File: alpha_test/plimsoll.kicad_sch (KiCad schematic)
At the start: 46 parts, among them J1 TAG CONNECT, J2 USB_C, J3 Loadd Cell, J4 Test Points, SW1 RESET, SW2 BOOT0, U1 USBLC6-2SC6, U2 APX803L20-29SA-7, U3 STM32F072RBTx, U4 AP2205-3.3, U5 RS3236-3.3, U6 HX717

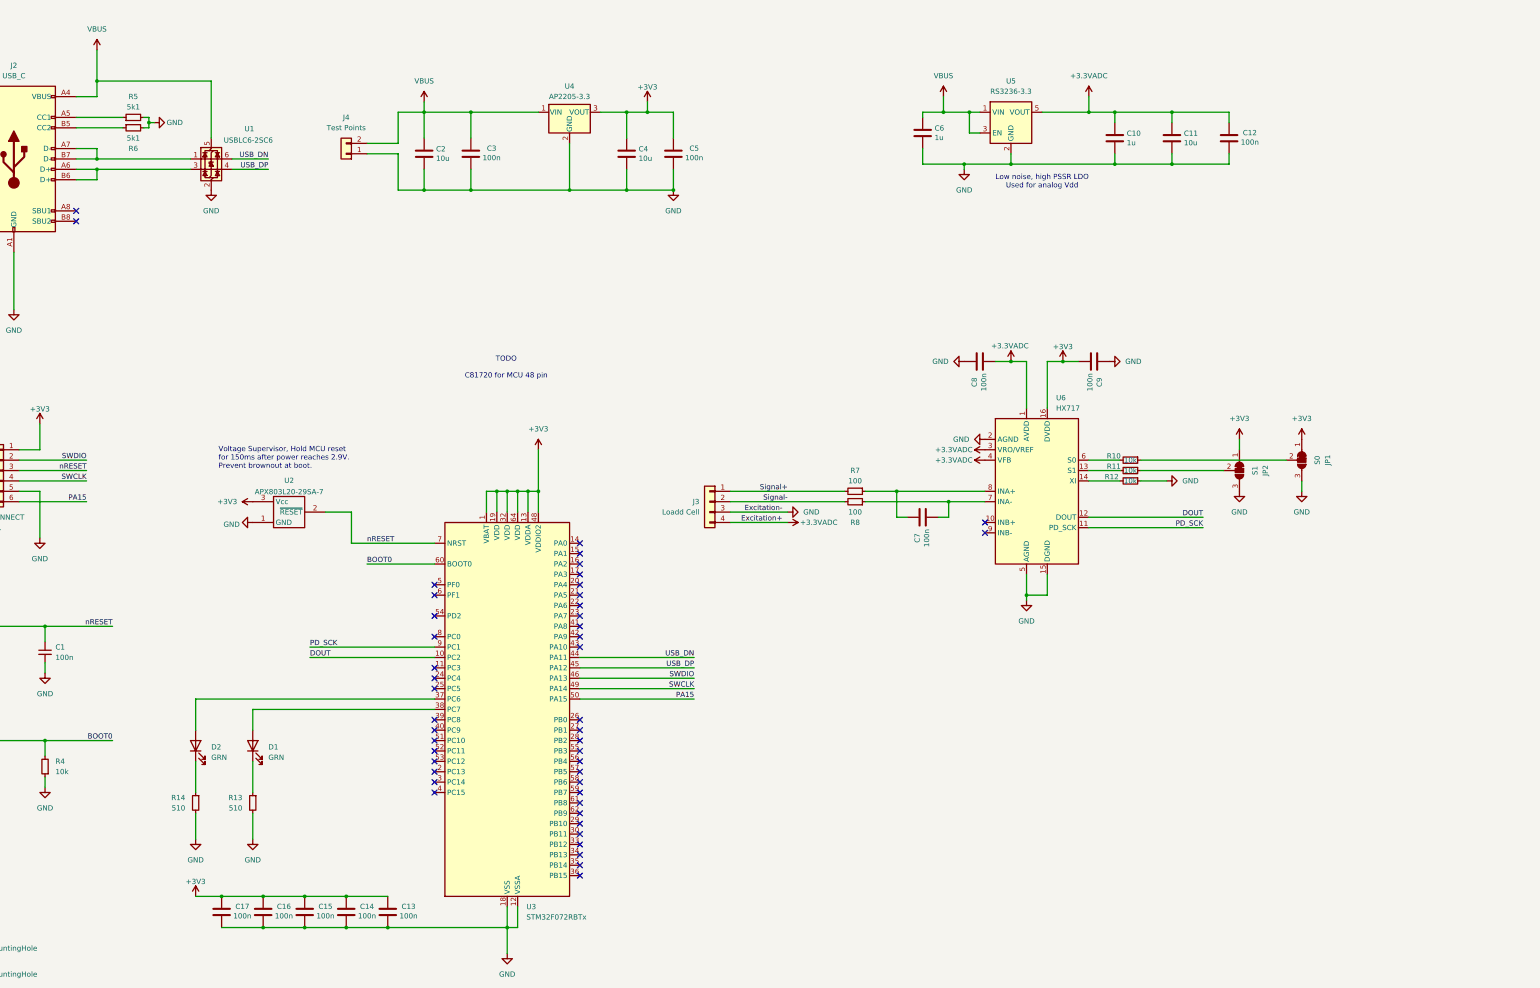
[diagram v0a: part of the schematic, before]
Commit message: updated alpha test for pcb to reuse parts from the alpha test
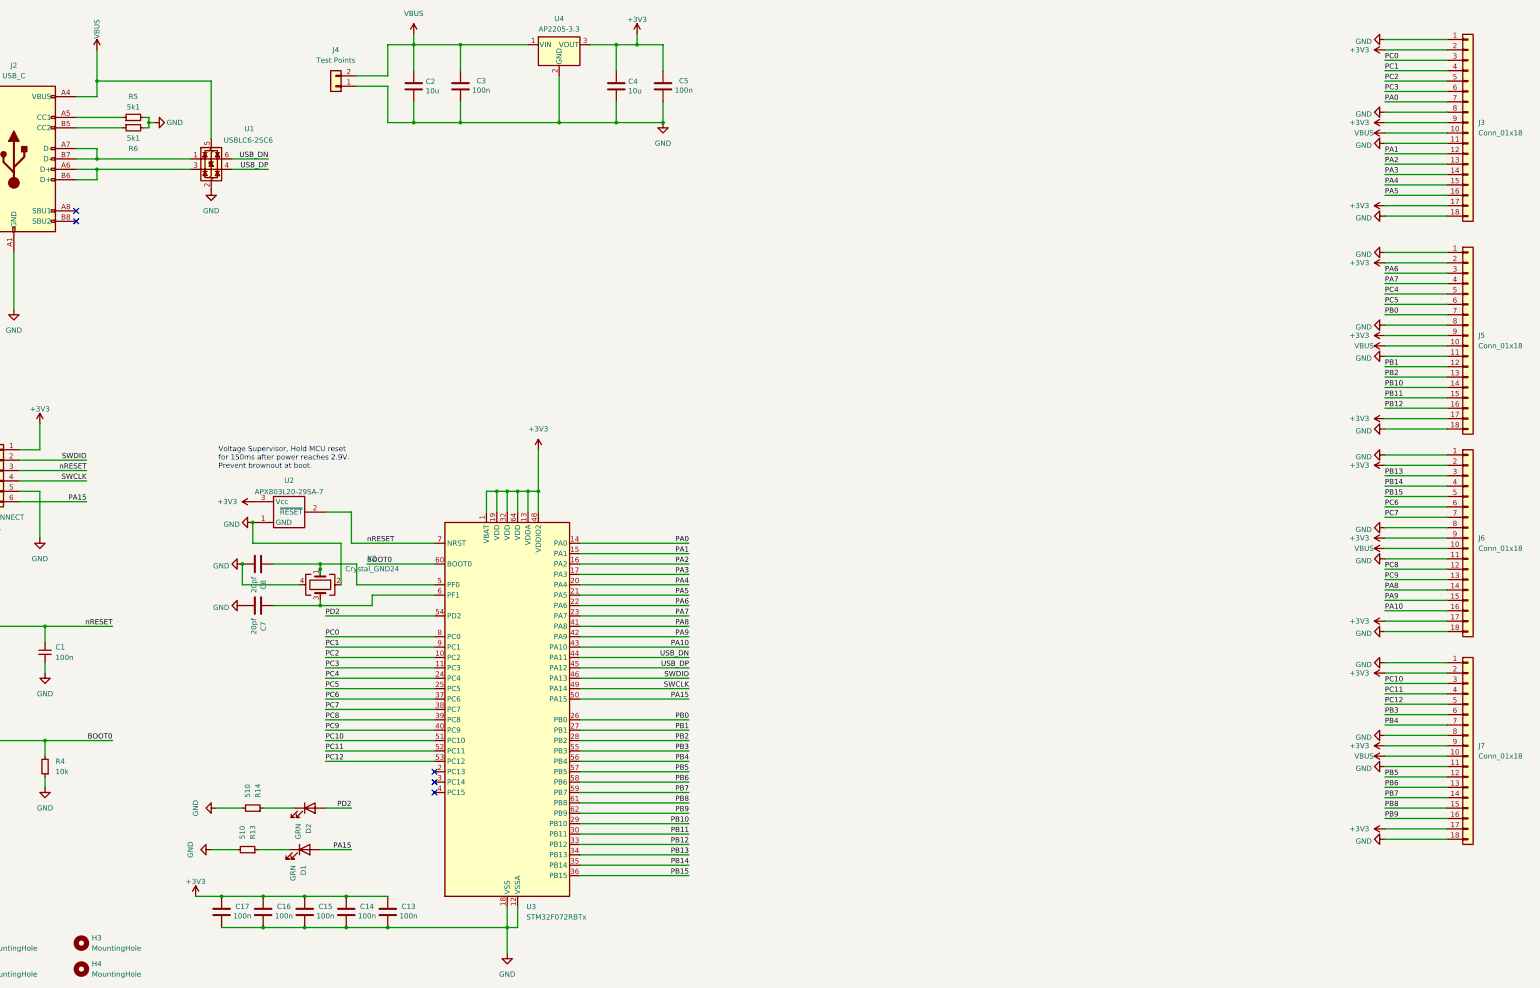
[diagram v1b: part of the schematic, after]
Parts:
- removed C10, C6: 1u, Capacitor_SMD:C_0805_2012Metric, symbol Device:C
- removed C11: 10u, Capacitor_SMD:C_0805_2012Metric, symbol Device:C
- removed C12, C9: 100n, Capacitor_SMD:C_0603_1608Metric, symbol Device:C
- removed J3: Loadd Cell, Connector_JST:JST_XH_B4B-XH-A_1x04_P2.50mm_Vertical, symbol Connector_Generic:Conn_01x04
- removed JP1: S0, Jumper:SolderJumper-3_P1.3mm_Bridged12_RoundedPad1.0x1.5mm_NumberLabels, symbol Jumper:SolderJumper_3_Bridged12
- removed JP2: S1, Jumper:SolderJumper-3_P1.3mm_Bridged12_RoundedPad1.0x1.5mm_NumberLabels, symbol Jumper:SolderJumper_3_Bridged12
- removed R10, R11, R12: 10k, Resistor_SMD:R_0603_1608Metric, symbol Device:R_Small
- removed R7, R8: 100, Resistor_SMD:R_0603_1608Metric, symbol Device:R_Small
- removed U5: RS3236-3.3, Package_TO_SOT_SMD:SOT-23-5, symbol Regulator_Linear:NCP163ASN350T1G
- removed U6: HX717, Package_SO:SOP-16_3.9x9.9mm_P1.27mm, symbol plimsoll-symbols:HX717
- added H3, H4: MountingHole, MountingHole:MountingHole_2.2mm_M2_ISO7380, symbol Mechanical:MountingHole
- added J3, J5, J6, J7: Conn_01x18, Connector_PinHeader_2.54mm:PinHeader_1x18_P2.54mm_Vertical, symbol Connector_Generic:Conn_01x18
- added Y2: Crystal_GND24, Crystal:Crystal_SMD_3225-4Pin_3.2x2.5mm_HandSoldering, symbol Device:Crystal_GND24
- C7, C8: value 100n -> 20pf
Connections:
- net +3.3VADC is gone; now on net GND: C8.1
- net +3V3: now also J3.17 (Pin_17), J3.2 (Pin_2), J3.9 (Pin_9), J5.17 (Pin_17), J5.2 (Pin_2), J5.9 (Pin_9), J6.17 (Pin_17), J6.2 (Pin_2), J6.9 (Pin_9), J7.17 (Pin_17), J7.2 (Pin_2), J7.9 (Pin_9)
- net GND: now also C7.1, J3.1 (Pin_1), J3.11 (Pin_11), J3.18 (Pin_18), J3.8 (Pin_8), J5.1 (Pin_1), J5.11 (Pin_11), J5.18 (Pin_18), J5.8 (Pin_8), J6.1 (Pin_1), J6.11 (Pin_11), J6.18 (Pin_18), J6.8 (Pin_8), J7.1 (Pin_1), J7.11 (Pin_11), J7.18 (Pin_18), J7.8 (Pin_8), Y2.2, Y2.4; no longer C8.2
- net PA15: now also D1.2 (A)
- net VBUS: now also J3.10 (Pin_10), J5.10 (Pin_10), J6.10 (Pin_10), J7.10 (Pin_10)
- net PC6: now reaches U3.37 (PC6)
- net PC6: now also J6.6 (Pin_6); no longer D2.2 (A)
- net at C7.2: now also U3.6 (PF1), Y2.3
- net PC3: now reaches U3.11 (PC3)
- net PC3: now also J3.6 (Pin_6)
- net PA0: now reaches U3.14 (PA0)
- net PA0: now also J3.7 (Pin_7)
- net PA1: now reaches U3.15 (PA1)
- net PA1: now also J3.12 (Pin_12)
- net PA2: now reaches U3.16 (PA2)
- net PA2: now also J3.13 (Pin_13)
- net PA3: now reaches U3.17 (PA3)
- net PA3: now also J3.14 (Pin_14)
- net PA4: now reaches U3.20 (PA4)
- net PA4: now also J3.15 (Pin_15)
- net PA5: now reaches U3.21 (PA5)
- net PA5: now also J3.16 (Pin_16)
- net PA6: now reaches U3.22 (PA6)
- net PA6: now also J5.3 (Pin_3)
- net PA7: now reaches U3.23 (PA7)
- net PA7: now also J5.4 (Pin_4)
- net PC4: now reaches U3.24 (PC4)
- net PC4: now also J5.5 (Pin_5)
- net PC5: now reaches U3.25 (PC5)
- net PC5: now also J5.6 (Pin_6)
- net PB0: now reaches U3.26 (PB0)
- net PB0: now also J5.7 (Pin_7)
- net PB1: now reaches U3.27 (PB1)
- net PB1: now also J5.12 (Pin_12)
- net PB2: now reaches U3.28 (PB2)
- net PB2: now also J5.13 (Pin_13)
- net PB10: now reaches U3.29 (PB10)
- net PB10: now also J5.14 (Pin_14)
- net PB11: now reaches U3.30 (PB11)
- net PB11: now also J5.15 (Pin_15)
- net PB12: now reaches U3.33 (PB12)
- net PB12: now also J5.16 (Pin_16)
- net PB13: now reaches U3.34 (PB13)
- net PB13: now also J6.3 (Pin_3)
- net PB14: now reaches U3.35 (PB14)
- net PB14: now also J6.4 (Pin_4)
- net PB15: now reaches U3.36 (PB15)
- net PB15: now also J6.5 (Pin_5)
- net PC7: now reaches U3.38 (PC7)
- net PC7: now also J6.7 (Pin_7); no longer D1.2 (A)
- net PC8: now reaches U3.39 (PC8)
- net PC8: now also J6.12 (Pin_12)
- net PC9: now reaches U3.40 (PC9)
- net PC9: now also J6.13 (Pin_13)
- net PA8: now reaches U3.41 (PA8)
- net PA8: now also J6.14 (Pin_14)
- net PA9: now reaches U3.42 (PA9)
- net PA9: now also J6.15 (Pin_15)
- net PA10: now reaches U3.43 (PA10)
- net PA10: now also J6.16 (Pin_16)
- net at U3.5 (PF0): now also C8.2, Y2.1
- net PC10: now reaches U3.51 (PC10)
- net PC10: now also J7.3 (Pin_3)
- net PC11: now reaches U3.52 (PC11)
- net PC11: now also J7.4 (Pin_4)
- net PC12: now reaches U3.53 (PC12)
- net PC12: now also J7.5 (Pin_5)
- net PD2: now reaches U3.54 (PD2)
- net PD2: now also D2.2 (A)
- net PB3: now reaches U3.55 (PB3)
- net PB3: now also J7.6 (Pin_6)
- net PB4: now reaches U3.56 (PB4)
- net PB4: now also J7.7 (Pin_7)
- net PB5: now reaches U3.57 (PB5)
- net PB5: now also J7.12 (Pin_12)
- net PB6: now reaches U3.58 (PB6)
- net PB6: now also J7.13 (Pin_13)
- net PB7: now reaches U3.59 (PB7)
- net PB7: now also J7.14 (Pin_14)
- net PB8: now reaches U3.61 (PB8)
- net PB8: now also J7.15 (Pin_15)
- net PB9: now reaches U3.62 (PB9)
- net PB9: now also J7.16 (Pin_16)
- net PC0: now reaches U3.8 (PC0)
- net PC0: now also J3.3 (Pin_3)
- net DOUT renamed PC2
- net PC2: now also J3.5 (Pin_5)
- net PD_SCK renamed PC1
- net PC1: now also J3.4 (Pin_4)
- no-connect marks 46 -> 5
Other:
- note removed: "Low noise, high PSSR LDO Used for analog Vdd"
- note removed: "TODO C81720 for MCU 48 pin"
- moved on the sheet: C2, C3, C4, C5, D1, D2, J4, R13, R14, U4
